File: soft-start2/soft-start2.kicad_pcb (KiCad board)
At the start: 2 copper layers, 61 x 84.8 mm, 55 parts, among them J10 Conn_01x02_Pin, J11 Conn_01x02_Socket, J3 Conn_01x01_Pin, J4 Conn_01x01_Pin, J5 Conn_01x01_Pin, J8 Conn_01x01_Pin, Q1 IRFB3004PbF, Q2 IRFB3004PbF, U1 P0102BL, U2 TLC555xD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

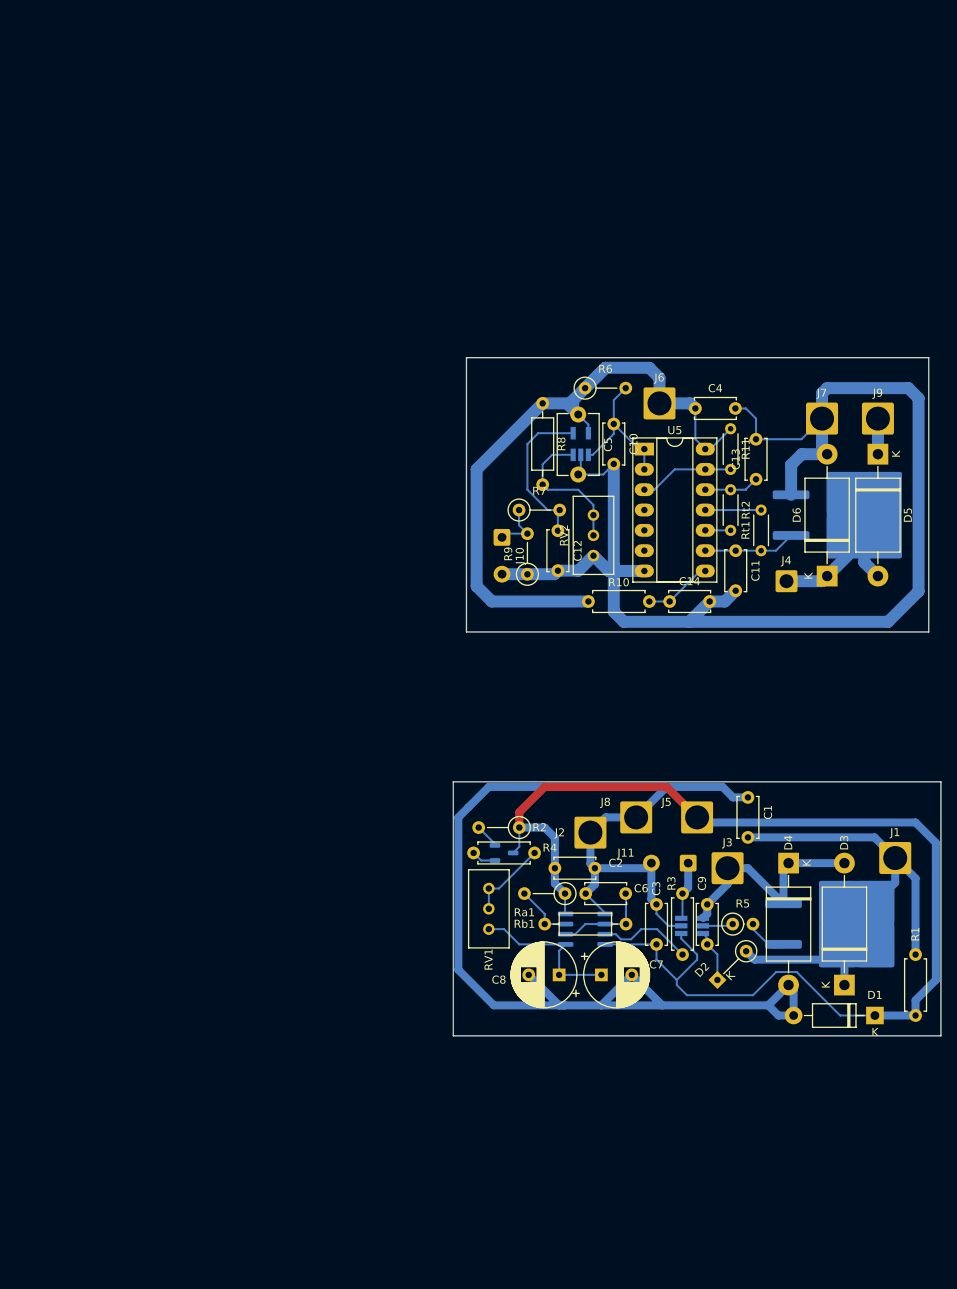
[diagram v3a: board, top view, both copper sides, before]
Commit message: [DRL] [soft-start] Update track widths. Prepare for plotting
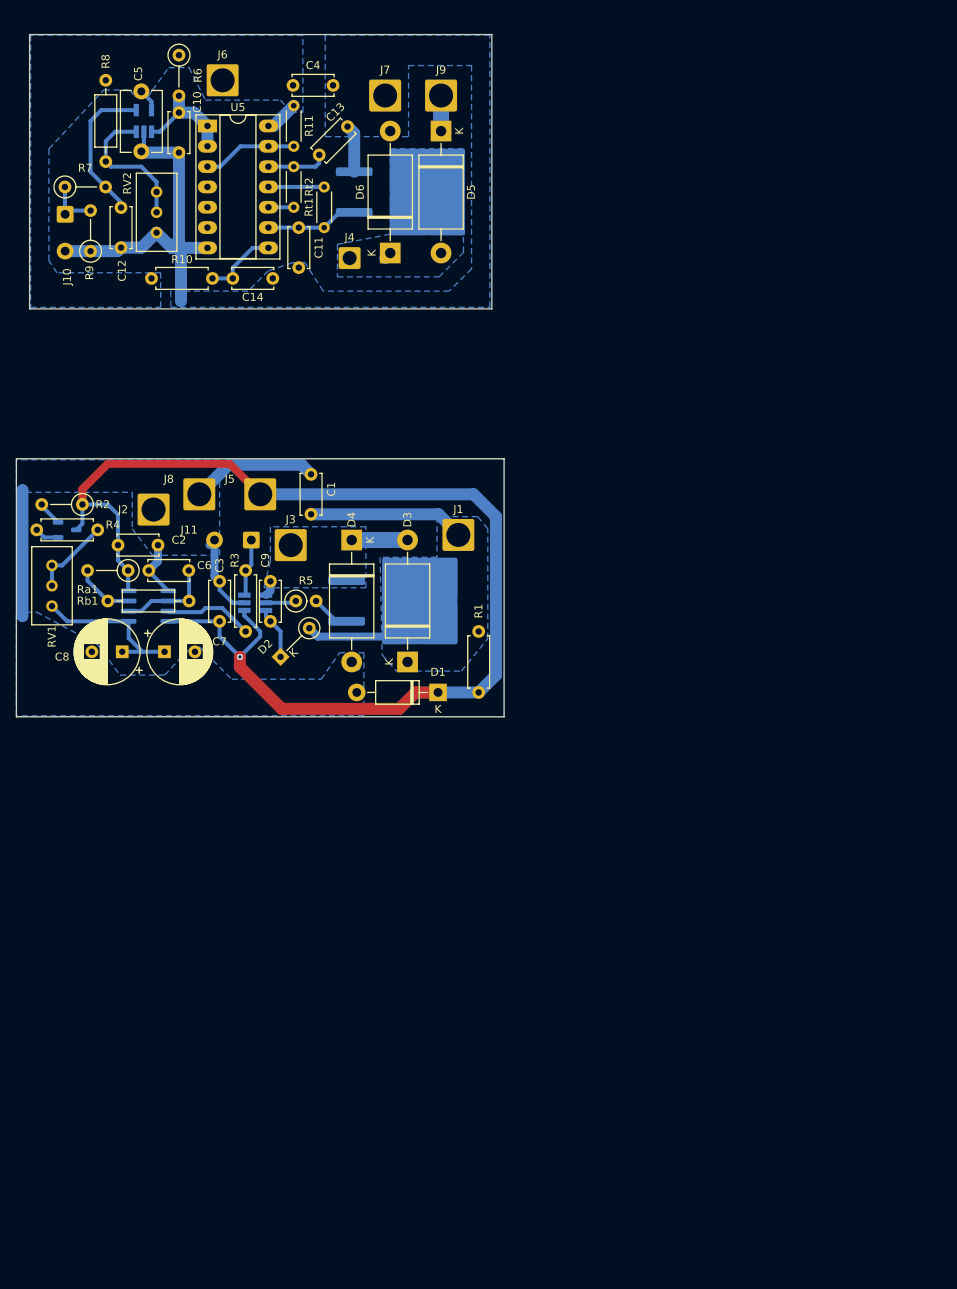
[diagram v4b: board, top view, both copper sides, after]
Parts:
- moved R7 69.7 mm to (23.8, 36.8)
- moved C13 68.0 mm to (55.6, 32.8), turned to 45 degrees
- moved R1 67.9 mm to (75.6, 92.3)
- moved C12 67.9 mm to (30.9, 39.3)
- moved D1 67.9 mm to (70.5, 99.9)
- moved D3 67.9 mm to (66.7, 96.1)
- moved D5 67.9 mm to (70.9, 29.8)
- moved J1 67.9 mm to (73.0, 80.3)
- moved J4 67.9 mm to (59.4, 45.7)
- moved J6 67.9 mm to (43.6, 23.4)
- moved R11 67.9 mm to (52.4, 26.6)
- moved R2 67.9 mm to (26.0, 76.5)
- moved R3 67.9 mm to (46.4, 92.3)
- moved R9 67.9 mm to (27.0, 44.8)
- moved Rt1 67.9 mm to (56.3, 41.8)
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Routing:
- net GND: track 168.9 -> 51.1 mm
- net GND2: track 162.8 -> 52.5 mm
- net VCC2: track 92.7 -> 8.06 mm
- net +BATT: track 56.8 -> 33.3 mm
- net Net-(D5-A2): track 23.2 -> 0.90 mm
- net /POWER_OUTPUT: track 28.7 -> 9.82 mm
- net Net-(C10-Pad1): track 18.3 -> 14.0 mm
- net /TRIGGER_RESET: track 8.58 -> 9.99 mm
- net /INT: track 19.8 -> 18.7 mm
- net Net-(Q1-G): track 6.50 -> 7.40 mm
- net Net-(U2-Q): track 11.8 -> 11.1 mm
- net VCC: track 153.4 -> 153.7 mm, vias 0 -> 1
- added copper zone on B.Cu, net +BATT
- added copper zone on B.Cu, net /POWER_OUTPUT
- added copper zone on B.Cu, net GND
- added copper zone on B.Cu, net GND2
- added copper zone on B.Cu, net Net-(D5-A2)
- added copper zone on B.Cu, net VCC2
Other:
- board size 61 x 84.8 mm -> 61 x 85.3 mm

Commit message: [soft-start] Reset PWM generator on trigger latch. Update plot settings
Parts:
- added J12: Conn_01x01_Pin, Connector_Wire:SolderWire-0.5sqmm_1x01_D0.9mm_OD2.1mm, F.Cu at (56.1, 26.2)
- added J13: Conn_01x01_Socket, Connector_Wire:SolderWire-0.5sqmm_1x01_D0.9mm_OD2.1mm, F.Cu at (43.9, 98.6)
- moved C4 4.76 mm to (52.4, 19.3)
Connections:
- net Net-(C13-Pad1) renamed /TRIGGER_OUT_INV
- U2 pad 4: VCC -> Net-(J13-Pin_1)
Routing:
- net Net-(J13-Pin_1): track 0.00 -> 11.8 mm
- net /TRIGGER_OUT_INV: track 7.40 -> 14.2 mm
- net VCC: track 153.7 -> 147.3 mm
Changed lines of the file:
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@@
     (pad_to_mask_clearance 0)
     (pcbplotparams
-      (layerselection 0x0000000_ffffffff)
+      (layerselection 0x0000000_fffffffe)
       (plot_on_all_layers_selection 0x0000000_00000000)
       (disableapertmacros false)
@@
       (subtractmaskfromsilk false)
       (outputformat 2)
-      (mirror true)
+      (mirror false)
       (drillshape 1)
       (scaleselection 1)
@@
   (net 11 "/INT")
   (net 12 "/U1_DISCH")
-  (net 13 "Net-(C13-Pad1)")
+  (net 13 "/TRIGGER_OUT_INV")
   (net 14 "Net-(D5-A2)")
   (net 15 "Net-(U1-G)")
@@
   (net 31 "VCC2")
   (net 32 "/PWM2")
+  (net 33 "Net-(J13-Pin_1)")
   (footprint "Potentiometer_THT:Potentiometer_Bourns_3296W_Vertical" (layer "F.Cu")
     (at 22.225 84.074 90)
@@
     )
   )
+  (footprint "Connector_Wire:SolderWire-0.5sqmm_1x01_D0.9mm_OD2.1mm" (layer "F.Cu")
+    (at 56.134 26.162)
+    (descr "Soldered wire connection, for a single 0.5 mm² wire, basic insulation, conductor diameter 0.9mm, outer diameter 2.1mm, size source Multi-Contact FLEXI-E 0.5 (https://ec.staubli.com/AcroFiles/Catalogues/TM_Cab-Main-11014119_(en)_hi.pdf), bend radius 3 times outer diameter, generated with kicad-footprint-generator")
+    (tags "connector wire 0.5sqmm")
+    (property "Sheetfile" "soft-start2.kicad_sch")
+    (property "Sheetname" "")
+    (property "ki_description" "Generic connector, single row, 01x01, script generated")
+    (property "ki_keywords" "connector")
+    (attr exclude_from_pos_files)
+    (fp_text reference "J12" (at 0 -2.25) (layer "F.SilkS")
+        (effects (font (size 1 1) (thickness 0.15)))
+    )
+    (fp_text value "Conn_01x01_Pin" (at 0 2.25) (layer "F.Fab")
+        (effects (font (size 1 1) (thickness 0.15)))
+    )
+    (fp_text user "${REFERENCE}" (at 0 0) (layer "F.Fab")
+        (effects (font (size 0.52 0.52) (thickness 0.08)))
+    )
+    (fp_line (start -1.8 -1.55) (end -1.8 1.55)
+      (stroke (width 0.05) (type solid)) (layer "F.CrtYd"))
+    (fp_line (start -1.8 1.55) (end 1.8 1.55)
+      (stroke (width 0.05) (type solid)) (layer "F.CrtYd"))
+    (fp_line (start 1.8 -1.55) (end -1.8 -1.55)
+      (stroke (width 0.05) (type solid)) (layer "F.CrtYd"))
+    (fp_line (start 1.8 1.55) (end 1.8 -1.55)
+      (stroke (width 0.05) (type solid)) (layer "F.CrtYd"))
+    (fp_circle (center 0 0) (end 1.05 0)
+      (stroke (width 0.1) (type solid)) (fill none) (layer "F.Fab"))
+    (pad "1" thru_hole roundrect (at 0 0) (size 2.1 2.1) (drill 1.1) (layers "*.Cu" "*.Mask") (roundrect_rratio 0.1190480952)
+      (net 13 "/TRIGGER_OUT_INV") (pinfunction "Pin_1") (pintype "passive"))
+    (model "${KICAD6_3DMODEL_DIR}/Connector_Wire.3dshapes/SolderWire-0.5sqmm_1x01_D0.9mm_OD2.1mm.wrl"
+      (offset (xyz 0 0 0))
+      (scale (xyz 1 1 1))
+      (rotate (xyz 0 0 0))
+    )
+  )
   (footprint "Capacitor_THT:C_Disc_D5.0mm_W2.5mm_P5.00mm" (layer "F.Cu")
     (at 49.53 91.059 90)
@@
   )
   (footprint "Capacitor_THT:C_Disc_D5.0mm_W2.5mm_P5.00mm" (layer "F.Cu")
-    (at 52.364 24.0665)
+    (at 52.364 19.304)
     (descr "C, Disc series, Radial, pin pitch=5.00mm, , diameter*width=5*2.5mm^2, Capacitor, http://cdn-reichelt.de/documents/datenblatt/B300/DS_KERKO_TC.pdf")
     (tags "C Disc series Radial pin pitch 5.00mm  diameter 5mm width 2.5mm Capacitor")
@@
     (property "ki_keywords" "cap capacitor")
     (attr through_hole)
-    (fp_text reference "C4" (at 2.5 -2.5) (layer "F.SilkS")
+    (fp_text reference "C4" (at 2.5 2.286) (layer "F.SilkS")
         (effects (font (size 1 1) (thickness 0.15)))
     )
@@
     )
   )
+  (footprint "Connector_Wire:SolderWire-0.5sqmm_1x01_D0.9mm_OD2.1mm" (layer "F.Cu")
+    (at 43.942 98.552)
+    (descr "Soldered wire connection, for a single 0.5 mm² wire, basic insulation, conductor diameter 0.9mm, outer diameter 2.1mm, size source Multi-Contact FLEXI-E 0.5 (https://ec.staubli.com/AcroFiles/Catalogues/TM_Cab-Main-11014119_(en)_hi.pdf), bend radius 3 times outer diameter, generated with kicad-footprint-generator")
+    (tags "connector wire 0.5sqmm")
+    (property "Sheetfile" "soft-start2.kicad_sch")
+    (property "Sheetname" "")
+    (property "ki_description" "Generic connector, single row, 01x01, script generated")
+    (property "ki_keywords" "connector")
+    (attr exclude_from_pos_files)
+    (fp_text reference "J13" (at 0 -2.25) (layer "F.SilkS")
+        (effects (font (size 1 1) (thickness 0.15)))
+    )
+    (fp_text value "Conn_01x01_Socket" (at 0 2.25) (layer "F.Fab")
+        (effects (font (size 1 1) (thickness 0.15)))
+    )
+    (fp_text user "${REFERENCE}" (at 0 0) (layer "F.Fab")
+        (effects (font (size 0.52 0.52) (thickness 0.08)))
+    )
+    (fp_line (start -1.8 -1.55) (end -1.8 1.55)
+      (stroke (width 0.05) (type solid)) (layer "F.CrtYd"))
+    (fp_line (start -1.8 1.55) (end 1.8 1.55)
+      (stroke (width 0.05) (type solid)) (layer "F.CrtYd"))
+    (fp_line (start 1.8 -1.55) (end -1.8 -1.55)
+      (stroke (width 0.05) (type solid)) (layer "F.CrtYd"))
+    (fp_line (start 1.8 1.55) (end 1.8 -1.55)
+      (stroke (width 0.05) (type solid)) (layer "F.CrtYd"))
+    (fp_circle (center 0 0) (end 1.05 0)
+      (stroke (width 0.1) (type solid)) (fill none) (layer "F.Fab"))
+    (pad "1" thru_hole roundrect (at 0 0) (size 2.1 2.1) (drill 1.1) (layers "*.Cu" "*.Mask") (roundrect_rratio 0.1190480952)
+      (net 33 "Net-(J13-Pin_1)") (pinfunction "Pin_1") (pintype "passive"))
+    (model "${KICAD6_3DMODEL_DIR}/Connector_Wire.3dshapes/SolderWire-0.5sqmm_1x01_D0.9mm_OD2.1mm.wrl"
+      (offset (xyz 0 0 0))
+      (scale (xyz 1 1 1))
+      (rotate (xyz 0 0 0))
+    )
+  )
   (footprint "Diode_THT:D_DO-35_SOD27_P5.08mm_Vertical_KathodeUp" (layer "F.Cu")
     (at 50.798863 95.505137 45)
@@
       (net 22 "Net-(Rt1-Pad2)") (pintype "output"))
     (pad "12" thru_hole oval (at 7.62 5.08) (size 2.4 1.6) (drill 0.8) (layers "*.Cu" "*.Mask")
-      (net 13 "Net-(C13-Pad1)") (pintype "input"))
+      (net 13 "/TRIGGER_OUT_INV") (pintype "input"))
     (pad "13" thru_hole oval (at 7.62 2.54) (size 2.4 1.6) (drill 0.8) (layers "*.Cu" "*.Mask")
       (net 24 "/TRIGGER_SET") (pintype "input"))
@@
       (stroke (width 0.1) (type solid)) (layer "F.Fab"))
     (pad "1" thru_hole circle (at 0 0 45) (size 1.6 1.6) (drill 0.8) (layers "*.Cu" "*.Mask")
-      (net 13 "Net-(C13-Pad1)") (pintype "passive"))
+      (net 13 "/TRIGGER_OUT_INV") (pintype "passive"))
     (pad "2" thru_hole circle (at 5 0 45) (size 1.6 1.6) (drill 0.8) (layers "*.Cu" "*.Mask")
       (net 29 "GND2") (pintype "passive"))
@@
       (stroke (width 0.1) (type solid)) (layer "F.Fab"))
     (pad "1" thru_hole circle (at 0 0 270) (size 1.4 1.4) (drill 0.7) (layers "*.Cu" "*.Mask")
-      (net 13 "Net-(C13-Pad1)") (pintype "passive"))
+      (net 13 "/TRIGGER_OUT_INV") (pintype "passive"))
     (pad "2" thru_hole oval (at 5.08 0 270) (size 1.4 1.4) (drill 0.7) (layers "*.Cu" "*.Mask")
       (net 23 "Net-(Rt2-Pad2)") (pintype "passive"))
@@
       (net 16 "Net-(U2-Q)") (pinfunction "Q") (pintype "output"))
     (pad "4" smd roundrect (at -2.475 -1.905 180) (size 1.95 0.6) (layers "B.Cu" "B.Paste" "B.Mask") (roundrect_rratio 0.25)
-      (net 1 "VCC") (pinfunction "R") (pintype "input"))
+      (net 33 "Net-(J13-Pin_1)") (pinfunction "R") (pintype "input"))
     (pad "5" smd roundrect (at 2.475 -1.905 180) (size 1.95 0.6) (layers "B.Cu" "B.Paste" "B.Mask") (roundrect_rratio 0.25)
       (net 4 "/U1_CONT") (pinfunction "CV") (pintype "input"))
@@
   (segment (start 31.749999 84.709) (end 31.749999 87.183999) (width 0.5) (layer "B.Cu") (net 1))
   (segment (start 26.035 76.454) (end 29.21 76.454) (width 0.5) (layer "B.Cu") (net 1))
-  (segment (start 43.18 91.059) (end 36.765 91.059) (width 0.5) (layer "B.Cu") (net 1))
   (segment (start 35.48 83.559) (end 34.33 84.709) (width 1) (layer "B.Cu") (net 2))
   (segment (start 34.33 84.709) (end 34.33 84.814) (width 0.5) (layer "B.Cu") (net 2))
@@
   (segment (start 26.669999 84.709) (end 26.669999 85.978999) (width 0.5) (layer "B.Cu") (net 12))
   (segment (start 49.2875 34.2265) (end 49.2825 34.2215) (width 0.5) (layer "B.Cu") (net 13))
+  (segment (start 56.134 26.162) (end 55.636233 26.659767) (width 0.5) (layer "B.Cu") (net 13))
   (segment (start 52.4475 34.2265) (end 49.2875 34.2265) (width 0.5) (layer "B.Cu") (net 13))
   (segment (start 52.4425 34.2215) (end 52.4475 34.2265) (width 0.25) (layer "B.Cu") (net 13))
+  (segment (start 55.636233 26.659767) (end 55.636233 32.755767) (width 0.5) (layer "B.Cu") (net 13))
   (segment (start 55.6225 32.9165) (end 55.6225 33.7855) (width 0.5) (layer "B.Cu") (net 13))
   (segment (start 55.6225 33.7855) (end 55.1815 34.2265) (width 0.5) (layer "B.Cu") (net 13))
@@
   (segment (start 23.847 36.7665) (end 23.847 40.155999) (width 0.5) (layer "B.Cu") (net 32))
   (segment (start 23.847 40.155999) (end 23.8725 40.181499) (width 0.5) (layer "B.Cu") (net 32))
+  (segment (start 38.989 91.059) (end 36.765 91.059) (width 0.5) (layer "B.Cu") (net 33))
+  (segment (start 43.942 98.552) (end 43.942 96.012) (width 0.5) (layer "B.Cu") (net 33))
+  (segment (start 43.942 96.012) (end 38.989 91.059) (width 0.5) (layer "B.Cu") (net 33))
   (zone (net 2) (net_name "GND") (layer "B.Cu") (hatch edge 0.5)
     (connect_pads yes (clearance 0.5))
@@
     (polygon
       (pts
-        (xy 56.388 30.48)
+        (xy 56.388 23.876)
+        (xy 57.912 23.876)
+        (xy 57.912 28.194)
+        (xy 57.912 28.448)
+        (xy 57.912 30.48)
         (xy 66.802 30.48)
         (xy 66.802 21.59)

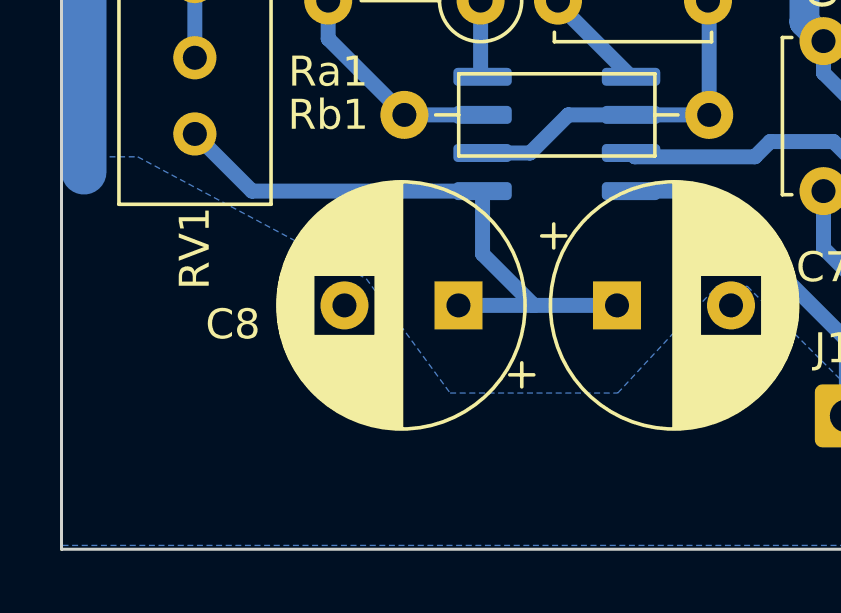
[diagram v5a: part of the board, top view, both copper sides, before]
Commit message: [soft-start] Add capacitor discharge resistor. It limits capacitor voltage to approx. 90% of VCC
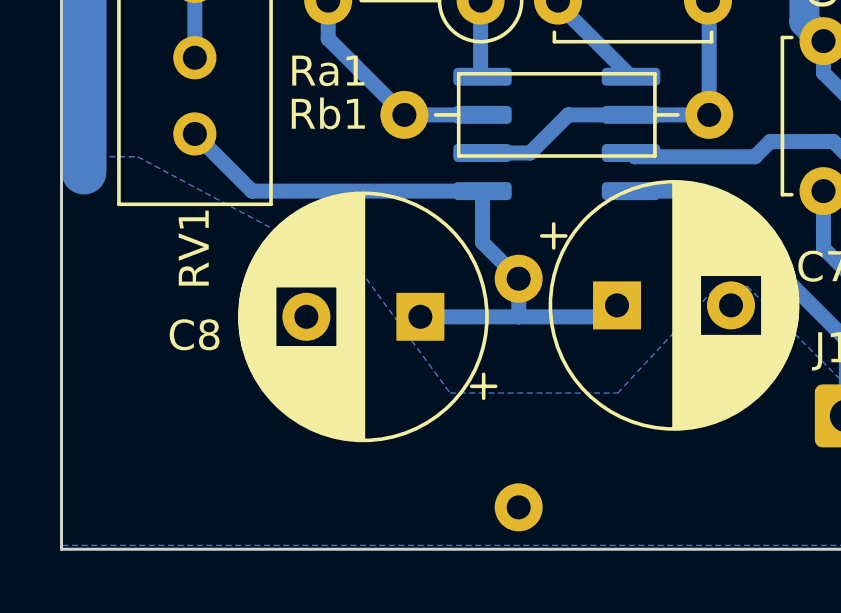
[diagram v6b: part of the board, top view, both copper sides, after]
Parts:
- added R12: 24k, Resistor_THT:R_Axial_DIN0207_L6.3mm_D2.5mm_P7.62mm_Horizontal, B.Cu at (33.0, 94.0)
- moved C8 1.33 mm to (29.7, 95.2)
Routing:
- net /U1_CONT: track 20.2 -> 21.8 mm
